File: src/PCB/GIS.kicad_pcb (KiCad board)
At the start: 2 copper layers, 132.5 x 101.3 mm, 85 parts, among them J1 LED, J2 4PIN, J3 OLED, SW1 SW_PUSH, SW10 SW_PUSH, SW11 SW_PUSH, SW12 SW_PUSH, SW13 SW_PUSH, SW14 SW_PUSH, SW15 SW_PUSH, SW16 SW_PUSH, SW17 SW_PUSH, SW18 SW_PUSH, SW19 SW_PUSH, SW2 SW_PUSH, SW20 SW_PUSH, SW21 SW_PUSH, SW22 SW_PUSH, SW23 SW_PUSH, SW24 SW_PUSH, SW26 SW_PUSH, SW27 SW_PUSH, SW28 SW_PUSH, SW29 SW_PUSH, SW3 SW_PUSH, SW30 SW_PUSH, SW4 SW_PUSH, SW5 SW_PUSH, SW6 SW_PUSH, SW7 SW_PUSH, SW8 SW_PUSH, SW9 SW_PUSH, U1 ProMicro

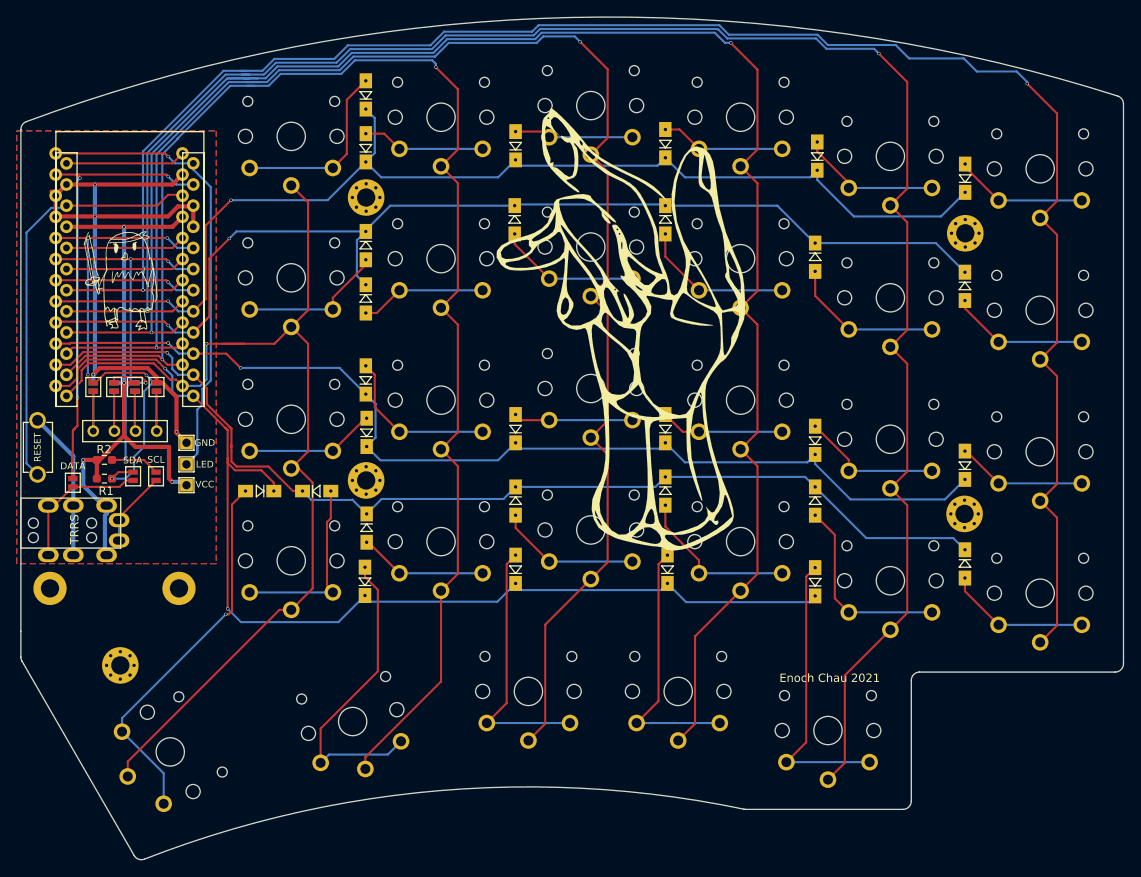
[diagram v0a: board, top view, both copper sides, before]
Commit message: fixing diode hole size
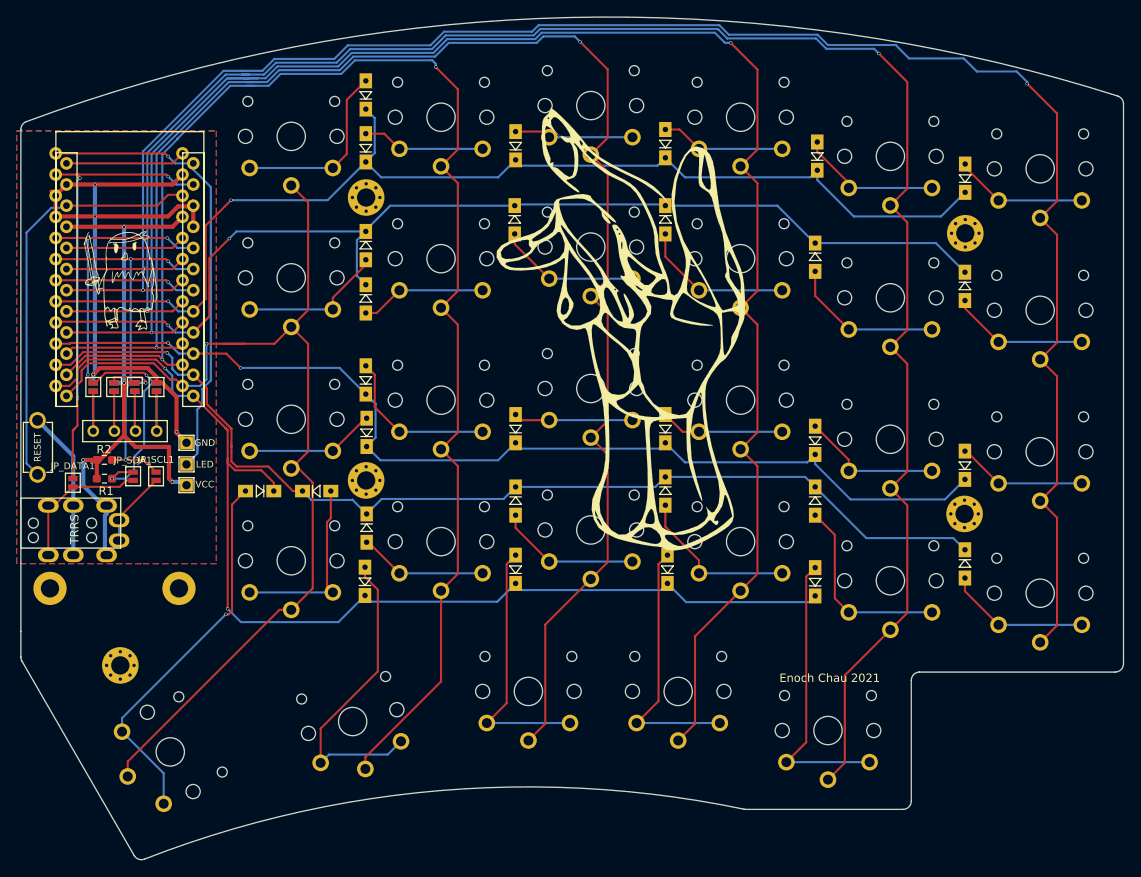
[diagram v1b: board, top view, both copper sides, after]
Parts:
- renumbered DATA to JP_DATA1, SCL to JP_SCL1, SDA to JP_SDA1

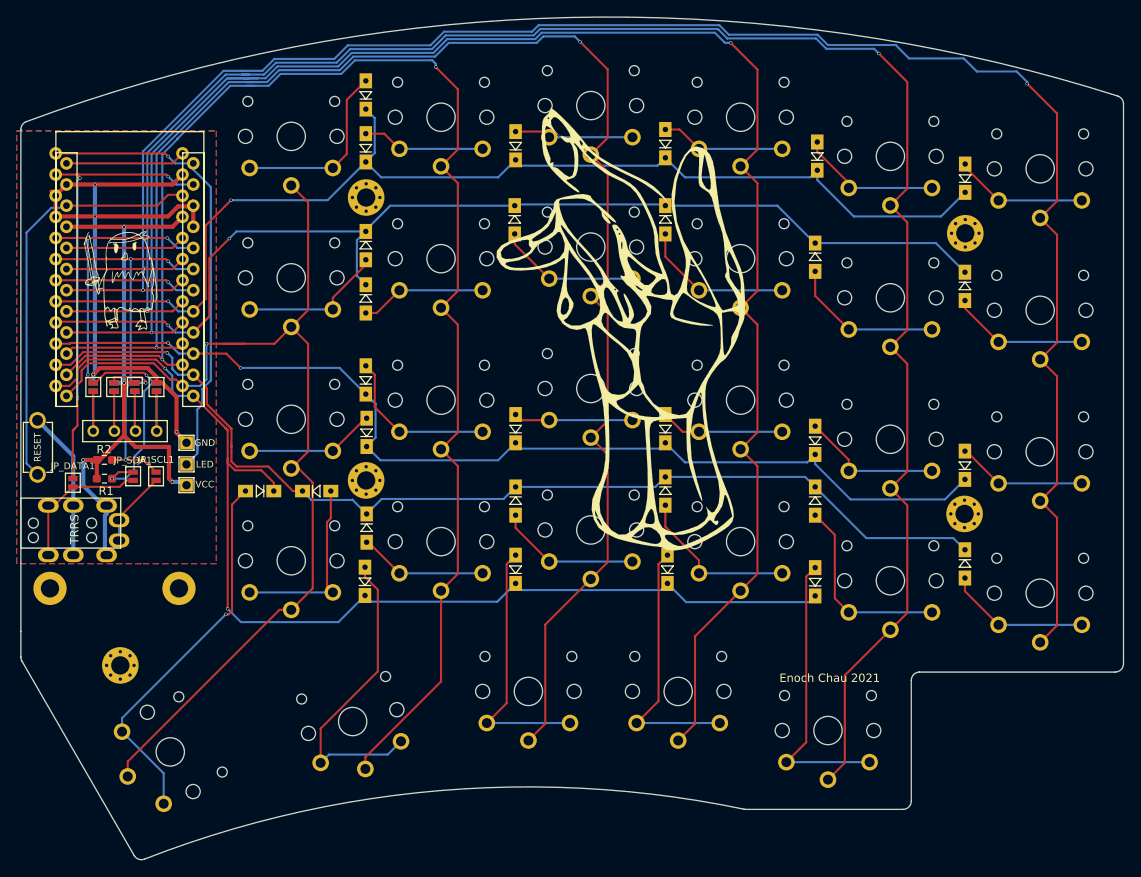
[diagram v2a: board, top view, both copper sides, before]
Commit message: switching to better dual diode footprint
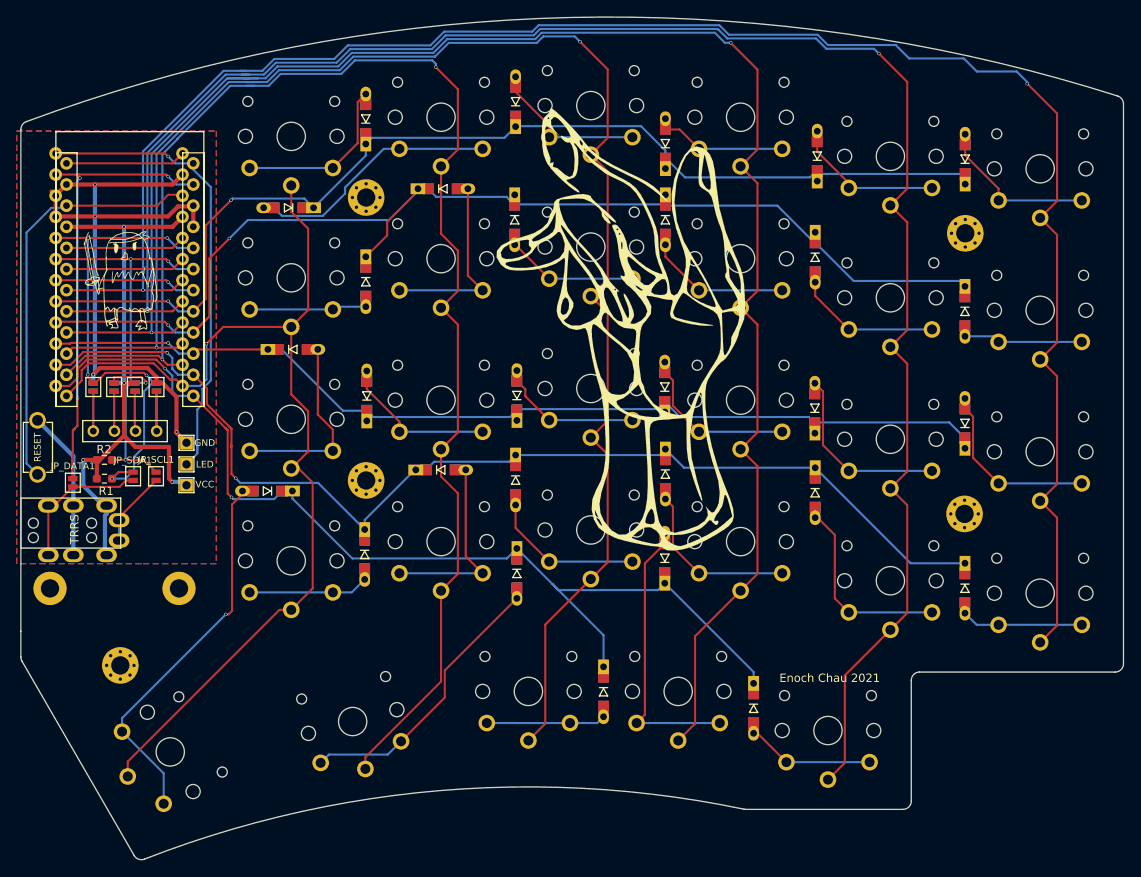
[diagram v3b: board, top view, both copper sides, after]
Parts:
- D1, D10, D11, D12, D13, D14, D15, D16, D17, D18, D19, D2, D20, D21, D22, D23, D24, D26, D27, D28, D29, D3, D30, D4, D5, D6, D7, D8, D9: footprint SofleKeyboard-footprint:Diode_SOD123 -> choc:D3_TH_SMD_v2
- moved D27 18.3 mm to (149.9, 104.9), turned to 270 degrees
- moved D28 18.1 mm to (160.3, 119.1), turned to 270 degrees
- moved D30 16.9 mm to (178.3, 121.1), turned to 270 degrees
- moved D8 16.2 mm to (141.0, 58.7), turned to 0 degrees
- moved D13 13.3 mm to (122.9, 78.0), turned to 0 degrees
- moved D2 11.7 mm to (122.4, 61.0), turned to 180 degrees
- moved D20 11.3 mm to (140.7, 92.5), turned to 0 degrees
- moved D19 9.56 mm to (131.6, 102.6), turned to 270 degrees
- moved D3 5.29 mm to (149.7, 48.2)
- moved D18 5.03 mm to (203.7, 86.9)
- moved D16 5.00 mm to (167.6, 82.5)
- moved D7 4.34 mm to (131.7, 69.8)
- moved D15 3.99 mm to (149.9, 83.5)
- moved D17 3.86 mm to (185.7, 85.0)
- moved D12 3.00 mm to (203.7, 73.4)
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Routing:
- net row3: track 128.2 -> 149.9 mm, vias 1 -> 2
- net row1: track 133.3 -> 153.7 mm
- net Net-(D30-Pad2): track 34.8 -> 17.8 mm
- net Net-(D2-Pad2): track 14.8 -> 31.7 mm
- net Net-(D28-Pad2): track 31.6 -> 16.8 mm
- net Net-(D20-Pad2): track 15.5 -> 25.7 mm
- net Net-(D8-Pad2): track 15.2 -> 25.4 mm
- net Net-(D13-Pad2): track 15.7 -> 25.4 mm
- net Net-(D17-Pad2): track 17.0 -> 24.7 mm
- net Net-(D18-Pad2): track 15.6 -> 23.1 mm
- net Net-(D3-Pad2): track 14.3 -> 21.4 mm
- net row0: track 137.5 -> 144.5 mm
- net Net-(D16-Pad2): track 14.9 -> 21.7 mm
- net Net-(D6-Pad2): track 16.0 -> 20.8 mm
- net Net-(D19-Pad2): track 22.7 -> 17.9 mm
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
